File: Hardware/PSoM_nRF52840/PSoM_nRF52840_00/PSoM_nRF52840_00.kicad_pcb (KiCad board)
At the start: 6 copper layers, 26.3 x 23.2 mm, 58 parts, among them J101 DF40C-60DP-0.4V(51), J102 Bare PCB USB C, SW401 SW_Push, SW402 SW_Push, U201 BQ24075RGTR, U301 MIC5528-3.3YMT-T5, U401 ESP32-S2FH4, Y601 Crystal_GND24_Small

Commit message: working on nrf52840
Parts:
- removed C201, C203: 4u7, Capacitor_SMD:C_0603_1608Metric
- removed C202: 1u, Capacitor_SMD:C_0603_1608Metric
- removed C301, C302: 2u2, Capacitor_SMD:C_0603_1608Metric
- removed C401, C402: 15p, Capacitor_SMD:C_0201_0603Metric
- removed C405, C408, C411, C412, C414, C415, C416: 100n, Capacitor_SMD:C_0201_0603Metric
- removed C406, C407: C, Capacitor_SMD:C_0201_0603Metric
- removed C409: 10u, Capacitor_SMD:C_0603_1608Metric
- removed C410, C413: 1u, Capacitor_SMD:C_0402_1005Metric
- removed R1, R2: R, Resistor_SMD:R_0402_1005Metric
- removed R103: 220k, Resistor_SMD:R_0201_0603Metric
- removed R104: 470k, Resistor_SMD:R_0201_0603Metric
- removed R201: 0, Resistor_SMD:R_0402_1005Metric
- removed R202: 36k5, Resistor_SMD:R_0402_1005Metric
- removed R203: 590, Resistor_SMD:R_0402_1005Metric
- removed R204: 1k1, Resistor_SMD:R_0402_1005Metric
- removed R205, R206: 1k5, Resistor_SMD:R_0402_1005Metric
- removed R207: 100k, Resistor_SMD:R_0402_1005Metric
- removed R301: 0k, Resistor_SMD:R_0201_0603Metric
- removed R401: 0, Resistor_SMD:R_0201_0603Metric
- removed R402: 2k, Resistor_SMD:R_0402_1005Metric
- removed R403, R404: 10k, Resistor_SMD:R_0201_0603Metric
- removed R405, R406, R407, R408: nu, Resistor_SMD:R_0201_0603Metric
- removed SW401, SW402: SW_Push, Component_lib:B3U-1000P
- removed U301: MIC5528-3.3YMT-T5, Component_lib:SON40P120X120X60-7N-D
- removed Y601: Crystal_GND24_Small, Component_lib:Crystal_SMD_2016-4Pin_2.0x1.6mm
- added ANT450: 2450AT18A100E, Component_lib:ANTC3216X140N, F.Cu at (163.7, 97.7)
- added C451: 1p, Capacitor_SMD:C_0201_0603Metric, F.Cu at (159.4, 90.2)
- added C461: 100n, Capacitor_SMD:C_0201_0603Metric, F.Cu at (159.4, 91.9)
- added D461: LED, LED_SMD:LED_0402_1005Metric, F.Cu at (172.4, 90.0)
- added L451: 3n9, Inductor_SMD:L_0201_0603Metric, F.Cu at (159.4, 95.4)
- added L452: 2n7, Inductor_SMD:L_0201_0603Metric, F.Cu at (159.4, 97.2)
- added R461: 10k, Resistor_SMD:R_0201_0603Metric, F.Cu at (159.4, 98.9)
- added R462: 2k, Resistor_SMD:R_0402_1005Metric, F.Cu at (172.2, 92.0)
- added SW461: SW_Push, Component_lib:B3U-1000P, F.Cu at (135.7, 106.0)
- added Y401: 830108161301, Component_lib:830108161301_1.6x1.2mm, F.Cu at (172.1, 87.4)
- C101: moved to F.Cu
- C403: value 100n -> 0p8; moved to F.Cu
- C404: value 100n -> 0p5; moved to F.Cu
- L401: value L -> 4n7
- R101: value 5.1k -> 220k; moved to F.Cu
- R102: value 5.1k -> 470k
- U201: value BQ24075RGTR -> NPM1300-QEAA-R; footprint Component_lib:QFN50P300X300X100-17N-D -> Component_lib:NPM1300-QEAA-R
- U401: value ESP32-S2FH4 -> nRF52840-QIAA-aQFN73; footprint Component_lib:QFN40P700X700X90-57N-D -> Component_lib:Nordic_AQFN-73-1EP_7x7mm_P0.5mm; moved to F.Cu
- moved R101 51.6 mm to (176.8, 89.3), turned to 0 degrees
- moved R102 51.0 mm to (176.8, 91.1), turned to 0 degrees
- moved C101 36.3 mm to (176.8, 87.6)
- moved U401 31.8 mm to (165.7, 90.8), turned to 0 degrees
- moved C403 30.8 mm to (159.4, 86.7), turned to 0 degrees
- moved C404 27.0 mm to (159.4, 88.4), turned to 0 degrees
- moved L401 24.0 mm to (159.4, 93.7), turned to 0 degrees
- moved U201 1.58 mm to (142.1, 95.0), turned to -135 degrees
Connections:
- C403 pad 1: +3V3 -> /400-nRF52840/LNA_IN
- C404 pad 1: +3V3 -> /400-nRF52840/ANT_IN
- J101 pad 14: /VSYS -> /100_Connectors/VSYS
- J101 pad 16: /VSYS -> /100_Connectors/VSYS
- J101 pad 28: /100_Connectors/EN -> /100_Connectors/RST
- J101 pad 4: /VBAT -> /100_Connectors/VBAT
- J101 pad 6: /VBAT -> /100_Connectors/VBAT
- J101 pad 8: /VBAT -> /100_Connectors/VBAT
- L401 pad 1: /400_ESP32/ANT -> /400-nRF52840/ANT_IN
- L401 pad 2: /400_ESP32/LNA_IN -> /400-nRF52840/LNA_IN
- R101 pad 1: /100_Connectors/CC2 -> /100_Connectors/VBAT
- R101 pad 2: GND -> IO1
- R102 pad 1: /100_Connectors/CC1 -> IO1
- U201 pad 1: /100_Connectors/BATTERY_TEMP -> /200_1S_Charger/3V3_nRF
- U201 pad 10: /VSYS -> unconnected-(U201-GPIO3-Pad10)
- U201 pad 11: /VSYS -> unconnected-(U201-GPIO4-Pad11)
- U201 pad 12: /200_1S_Charger/ILIM -> /200_1S_Charger/3V3_nRF
- U201 pad 13: VBUS -> /200_1S_Charger/SDA
- U201 pad 14: /200_1S_Charger/TMR -> /200_1S_Charger/SCL
- U201 pad 15: /200_1S_Charger/SYSOFF -> Net-(U201-SHPHLD)
- U201 pad 16: /200_1S_Charger/ISET -> Net-(U201-VSET2)
- U201 pad 17: GND -> Net-(U201-VSET1)
- U201 pad 2: /VBAT -> GND
- U201 pad 3: /VBAT -> /200_1S_Charger/SW1
- U201 pad 4: /200_1S_Charger/BQ_CE -> /100_Connectors/VSYS
- U201 pad 5: /200_1S_Charger/EN2 -> /200_1S_Charger/SW2
- U201 pad 6: /200_1S_Charger/EN1 -> GND
- U201 pad 7: /200_1S_Charger/BQ_PGOOD -> unconnected-(U201-GPIO0-Pad7)
- U201 pad 8: GND -> unconnected-(U201-GPIO1-Pad8)
- U201 pad 9: /200_1S_Charger/BQ_CHG -> unconnected-(U201-GPIO2-Pad9)
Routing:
- net GND: track 96.0 -> 22.2 mm, vias 71 -> 11
- net /VSYS: track 38.2 -> 0.00 mm, vias 4 -> 0
- net +3V3: track 36.4 -> 0.00 mm, vias 13 -> 0
- net VBUS: track 48.9 -> 17.1 mm, vias 5 -> 0
- net /VBAT: track 26.9 -> 0.00 mm, vias 4 -> 0
- net /100_Connectors/EN: track 21.9 -> 0.00 mm, vias 3 -> 0
- net IO15: track 20.4 -> 0.00 mm, vias 2 -> 0
- net IO41: track 17.8 -> 0.00 mm
- net IO40: track 17.6 -> 0.00 mm
- net IO0: track 17.0 -> 0.00 mm, vias 2 -> 0
- net /100_Connectors/RX0: track 16.7 -> 0.00 mm, vias 2 -> 0
- net IO39: track 16.3 -> 0.00 mm
- net /100_Connectors/TX0: track 15.9 -> 0.00 mm, vias 2 -> 0
- net IO37: track 15.3 -> 0.00 mm
- net IO38: track 15.3 -> 0.00 mm
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- removed copper zone on F.Cu, net +3V3
- removed copper zone on In2.Cu, net +3V3
- removed copper zone on F.Cu, net /VBAT
- removed copper zone on F.Cu, net /VSYS
- removed copper zone on B.Cu, net GND
- removed copper zone on F.Cu, net GND

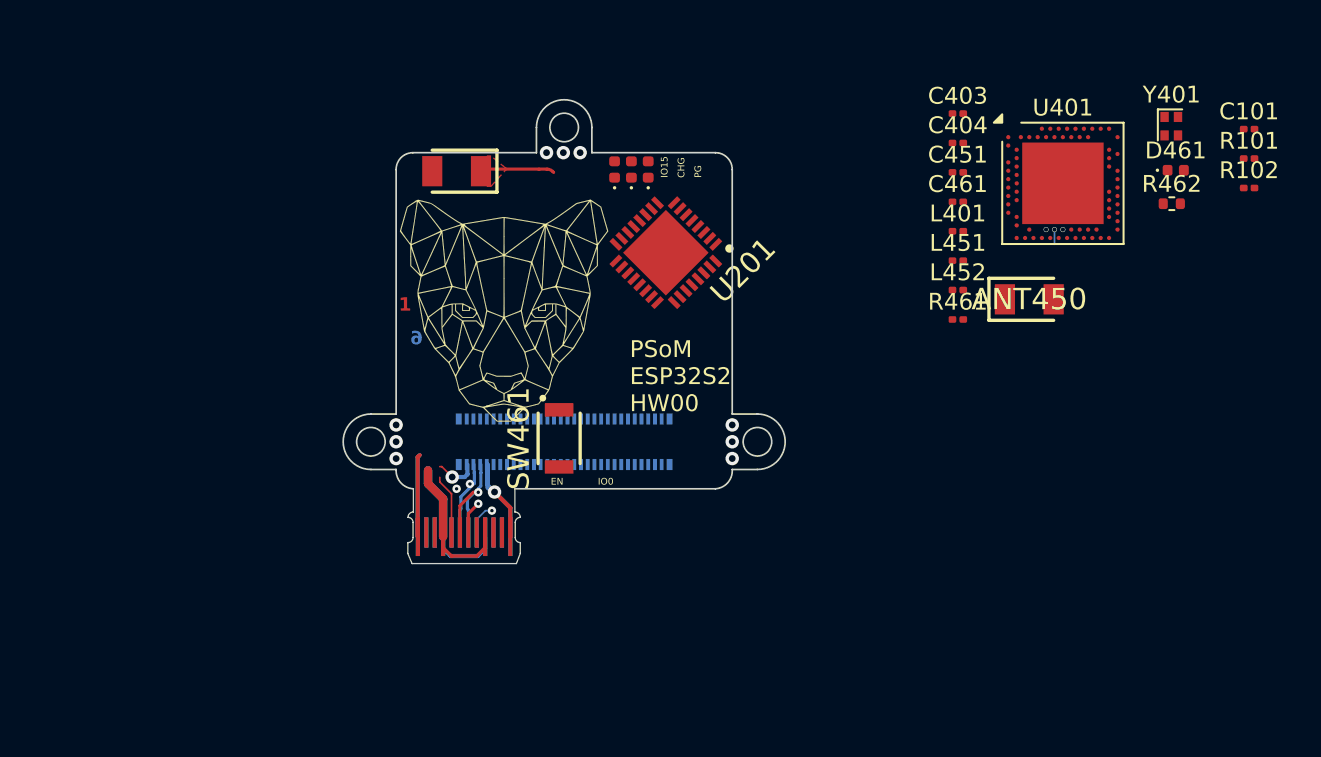
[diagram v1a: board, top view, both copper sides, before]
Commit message: footprint assignement done
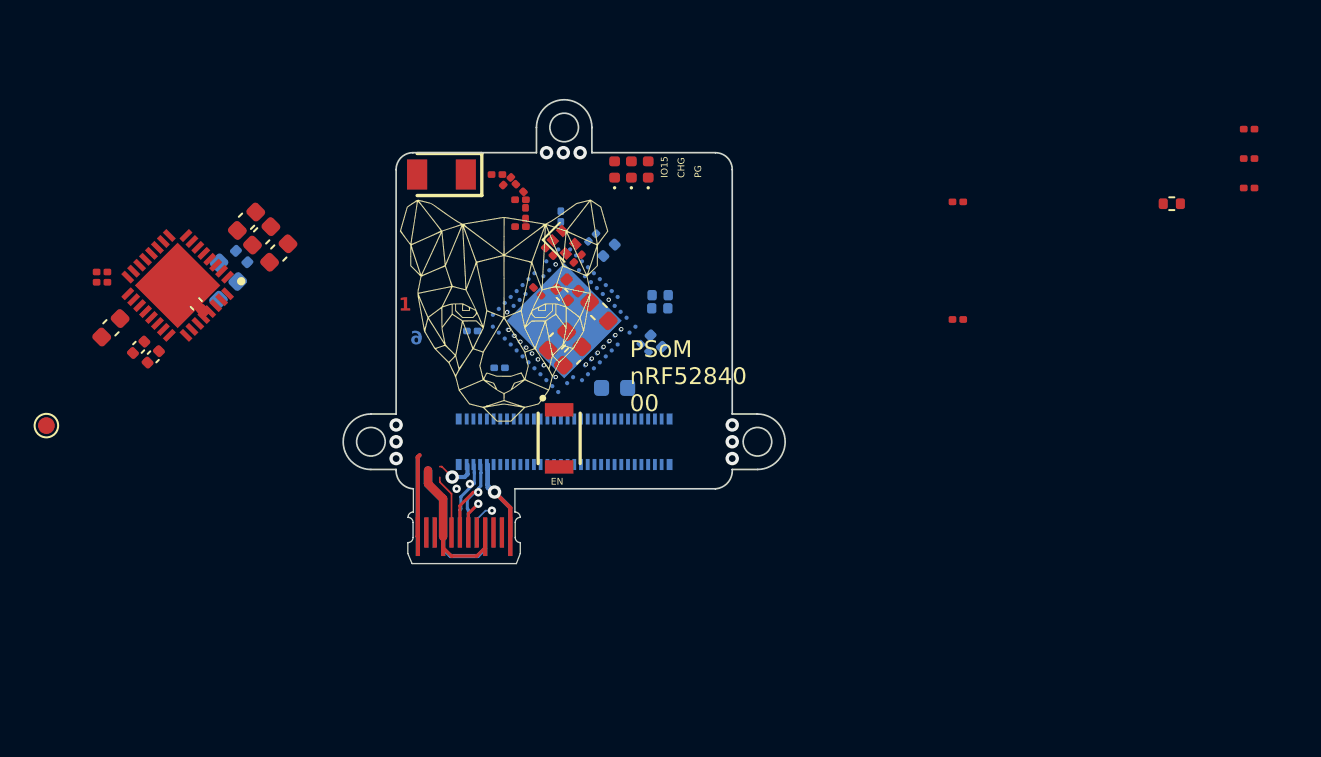
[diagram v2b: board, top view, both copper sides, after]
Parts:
- removed ANT401: 2450AT18A100E, Component_lib:ANTC3216X140N
- removed D401: LED, LED_SMD:LED_0402_1005Metric
- added C201: 1u, Capacitor_SMD:C_0402_1005Metric, F.Cu at (110.7, 100.6)
- added C202: 10u, Capacitor_SMD:C_0603_1608Metric, F.Cu at (117.1, 93.1)
- added C203: 10u, Capacitor_SMD:C_0603_1608Metric, F.Cu at (118.0, 94.0)
- added C204: 10u, Capacitor_SMD:C_0603_1608Metric, F.Cu at (119.0, 95.0)
- added C205: 1u, Capacitor_SMD:C_0402_1005Metric, F.Cu at (111.5, 101.2)
- added C206: 2u2, Capacitor_SMD:C_0603_1608Metric, F.Cu at (109.0, 99.4)
- added C207: 10u, Capacitor_SMD:C_0402_1005Metric, B.Cu at (116.8, 95.2)
- added C208: 10u, Capacitor_SMD:C_0402_1005Metric_Pad0.74x0.62mm_HandSolder, F.Cu at (114.1, 98.0)
- added C401: 12p, Capacitor_SMD:C_0201_0603Metric, F.Cu at (135.1, 94.9)
- added C402: 12p, Capacitor_SMD:C_0201_0603Metric, F.Cu at (136.8, 95.3)
- added C405: 100n, Capacitor_SMD:C_0201_0603Metric, B.Cu at (140.8, 100.6)
- added C406: 4u7, Capacitor_SMD:C_0603_1608Metric, B.Cu at (139.0, 103.0)
- added C407: 100n, Capacitor_SMD:C_0201_0603Metric, B.Cu at (132.2, 101.8)
- added C408: 100n, Capacitor_SMD:C_0201_0603Metric, B.Cu at (130.5, 99.6)
- added C409: 820p, Capacitor_SMD:C_0201_0603Metric, F.Cu at (134.4, 97.2)
- added C410: nc, Capacitor_SMD:C_0402_1005Metric, F.Cu at (135.9, 97.5)
- added C411: 100p, Capacitor_SMD:C_0201_0603Metric, B.Cu at (135.8, 92.8)
- added C412: 100n, Capacitor_SMD:C_0201_0603Metric, B.Cu at (137.7, 94.0)
- added C413: nc, Capacitor_SMD:C_0402_1005Metric, B.Cu at (138.7, 94.8)
- added C414: 1u, Capacitor_SMD:C_0402_1005Metric, B.Cu at (141.5, 100.2)
- added C415: 1u, Capacitor_SMD:C_0402_1005Metric, B.Cu at (141.7, 98.3)
- added C416: 47n, Capacitor_SMD:C_0402_1005Metric, B.Cu at (141.7, 97.5)
- added C420: 4u7, Capacitor_SMD:C_0603_1608Metric, F.Cu at (135.6, 100.2)
- added C421: 4u7, Capacitor_SMD:C_0603_1608Metric, F.Cu at (136.5, 101.1)
- added L201: 2u2, Inductor_SMD:L_0603_1608Metric, B.Cu at (116.0, 96.1)
- added L202: 2u2, Inductor_SMD:L_0603_1608Metric, B.Cu at (114.9, 97.2)
- added L402: 10u, Inductor_SMD:L_0603_1608Metric, F.Cu at (138.1, 98.5)
- added L403: 15n, Inductor_SMD:L_0402_1005Metric, F.Cu at (136.5, 96.9)
- added R203: 47k, Resistor_SMD:R_0201_0603Metric, F.Cu at (108.5, 96.7)
- added R204: 470k, Resistor_SMD:R_0201_0603Metric, F.Cu at (108.5, 96.1)
- added SHIPHLD1: TestPoint, TestPoint:TestPoint_Pad_D1.0mm, F.Cu at (105.2, 105.2)
- U401: moved to B.Cu
- moved Y401 36.8 mm to (136.0, 94.3), turned to 45 degrees
- moved ANT450 35.8 mm to (128.7, 90.3), turned to 180 degrees
- moved D461 33.4 mm to (139.0, 90.0), turned to 90 degrees
- moved U401 30.8 mm to (136.0, 99.0), turned to 135 degrees
- moved U201 29.1 mm to (113.0, 96.9)
- moved L451 27.9 mm to (132.0, 90.3)
- moved L452 27.6 mm to (132.6, 90.7), turned to -135 degrees
- moved C403 26.9 mm to (133.4, 93.4), turned to 180 degrees
- moved C404 26.2 mm to (133.4, 91.8), turned to 180 degrees
- moved C451 26.1 mm to (133.3, 91.1), turned to -45 degrees
- moved L401 25.7 mm to (133.7, 92.6), turned to -90 degrees
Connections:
- U401 pad A10: unconnected-(U401-AIN5/P0.29-PadA10) -> /400-nRF52840/P25
- U401 pad A14: unconnected-(U401-P1.15-PadA14) -> /400-nRF52840/P33
- U401 pad A16: unconnected-(U401-P1.13-PadA16) -> /400-nRF52840/P29
- U401 pad A20: unconnected-(U401-P1.10-PadA20) -> /400-nRF52840/P23
- U401 pad A8: unconnected-(U401-AIN7/P0.31-PadA8) -> /400-nRF52840/P27
- U401 pad G1: unconnected-(U401-P0.26-PadG1) -> /400-nRF52840/P30
- U401 pad H2: unconnected-(U401-P0.27-PadH2) -> /400-nRF52840/P32
- U401 pad R1: unconnected-(U401-TRACEDATA3/P1.09-PadR1) -> /400-nRF52840/P39
- U401 pad U24: unconnected-(U401-P1.04-PadU24) -> /400-nRF52840/P31
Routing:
- net /400_ESP32/ANT: track 4.43 -> 0.00 mm
- net /400-nRF52840/P38: track 0.94 -> 0.04 mm
- net /400-nRF52840/P35: track 0.00 -> 0.08 mm, vias 0 -> 1
- net /400-nRF52840/P11: track 0.00 -> 0.08 mm, vias 0 -> 1
- net /400-nRF52840/P7: track 0.00 -> 0.07 mm, vias 0 -> 1
- net /400-nRF52840/P21: track 0.00 -> 0.07 mm, vias 0 -> 1
- net /400-nRF52840/P44: track 0.00 -> 0.07 mm, vias 0 -> 1
- net /400-nRF52840/P32: track 0.00 -> 0.06 mm, vias 0 -> 1
- net SPI4: track 0.00 -> 0.06 mm, vias 0 -> 1
- net /400-nRF52840/P15: track 0.00 -> 0.06 mm, vias 0 -> 1
- net SPI5: track 0.00 -> 0.06 mm, vias 0 -> 1
- net /400-nRF52840/P46: track 0.00 -> 0.05 mm, vias 0 -> 1
- net /400-nRF52840/P13: track 0.00 -> 0.05 mm, vias 0 -> 1
- net SPI2: track 0.00 -> 0.05 mm, vias 0 -> 1
- net /400-nRF52840/DECUSB: track 0.00 -> 0.03 mm, vias 0 -> 1
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- removed copper zone on F.Cu, net /400_ESP32/ANT
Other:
- board text added: "PSoM nRF52840 00"
- board text removed: "IO0"
- board text removed: "PSoM ESP32S2 HW00"

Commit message: working on schematic
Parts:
- C207, C411, L201, L202: moved to F.Cu
- moved C411 24.4 mm to (143.6, 115.9), turned to -45 degrees
- moved C409 21.3 mm to (141.6, 117.3)
- moved L402 21.0 mm to (144.8, 118.3)
- moved C410 20.8 mm to (142.5, 117.2)
- moved C401 20.8 mm to (142.4, 114.4)
- moved C405 20.8 mm to (148.1, 120.1)
- moved C406 20.8 mm to (146.3, 122.5)
- moved C407 20.8 mm to (139.5, 121.3)
- moved C408 20.8 mm to (137.8, 119.1)
- moved C412 20.8 mm to (145.0, 113.5)
- moved C413 20.8 mm to (146.0, 114.3)
- moved C414 20.8 mm to (148.8, 119.7)
- moved C415 20.8 mm to (149.0, 117.8)
- moved U401 20.8 mm to (143.3, 118.5)
- moved Y401 20.8 mm to (143.3, 113.8)
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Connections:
- net Net-(U201-SHPHLD) renamed /200_1S_Charger/SHIP
- net Net-(U201-VSET1) renamed /200_1S_Charger/VSET1
- net Net-(U201-VSET2) renamed /200_1S_Charger/VSET2
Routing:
- net /200_1S_Charger/3V3_nRF: track 0.00 -> 10.4 mm
- net /100_Connectors/VSYS: track 0.00 -> 6.35 mm
- net /400-nRF52840/DEC4_6: track 0.00 -> 5.07 mm, vias 0 -> 1
- net /200_1S_Charger/VBUS_OUT: track 0.00 -> 3.70 mm, vias 0 -> 1
- net /200_1S_Charger/SW2: track 0.00 -> 3.31 mm
- net /200_1S_Charger/SW1: track 0.00 -> 3.25 mm
- net /100_Connectors/VBAT: track 0.00 -> 2.04 mm
- net /400-nRF52840/DECUSB: track 0.03 -> 2.05 mm
- net /400-nRF52840/DCC: track 0.00 -> 1.90 mm, vias 0 -> 1
- net /200_1S_Charger/VSET1: track 0.00 -> 1.68 mm
- net VBUS: track 17.1 -> 18.6 mm
- net /400-nRF52840/XC2: track 0.00 -> 1.36 mm, vias 0 -> 1
- net /100_Connectors/CC1: track 3.57 -> 4.91 mm
- net /100_Connectors/BATTERY_TEMP: track 0.00 -> 1.33 mm
- net /400-nRF52840/XC1: track 0.00 -> 1.31 mm, vias 0 -> 1
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
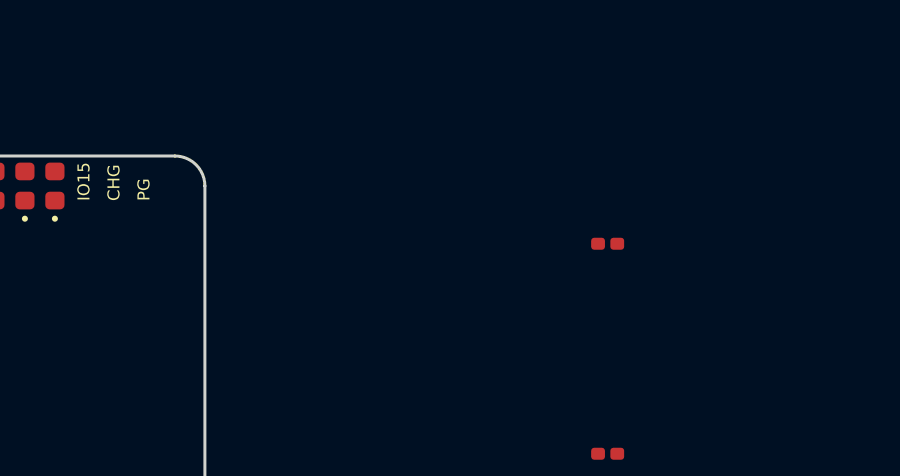
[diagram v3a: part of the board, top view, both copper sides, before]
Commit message: added nfc connector + update pinout info
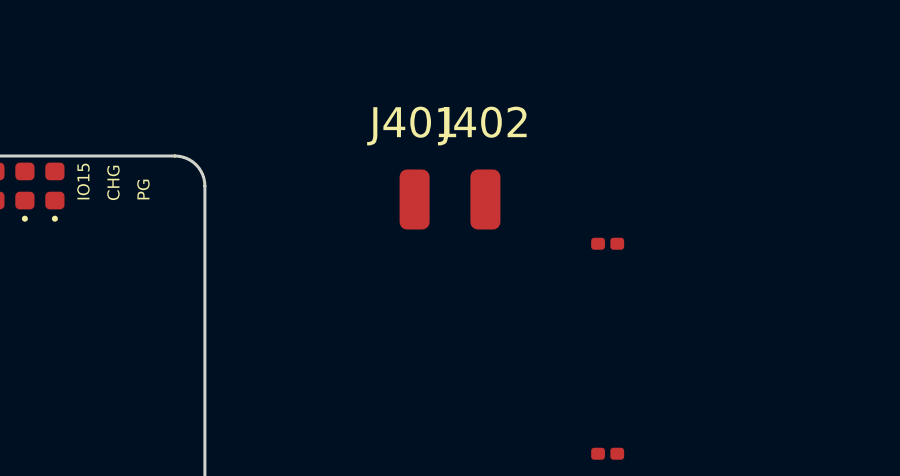
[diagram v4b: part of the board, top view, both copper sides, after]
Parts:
- added J401: Conn_01x01_Pin, Connector_Wire:SolderWirePad_1x01_SMD_1x2mm, F.Cu at (153.0, 90.5)
- added J402: Conn_01x01_Pin, Connector_Wire:SolderWirePad_1x01_SMD_1x2mm, F.Cu at (155.3, 90.5)
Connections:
- net IO0 renamed /100_Connectors/IO0
- C461 pad 1: SPI3 -> /100_Connectors/RST
- J101 pad 11: IO5 -> P11
- J101 pad 13: IO6 -> P13
- J101 pad 15: IO7 -> P15
- J101 pad 17: IO8 -> P17
- J101 pad 19: IO9 -> P19
- J101 pad 21: IO10 -> P21
- J101 pad 23: IO11 -> P23
- J101 pad 25: IO12 -> P25
- J101 pad 27: IO13 -> P27
- J101 pad 29: IO14 -> P29
- J101 pad 30: IO33 -> P30
- J101 pad 31: IO15 -> P31
- J101 pad 32: IO34 -> P32
- J101 pad 33: IO16 -> P33
- J101 pad 34: IO35 -> P34
- J101 pad 35: IO17 -> P35
- J101 pad 36: IO36 -> P36
- J101 pad 37: IO18 -> P37
- J101 pad 38: IO37 -> P38
- J101 pad 39: IO21 -> P39
- J101 pad 40: IO38 -> P40
- J101 pad 42: IO41 -> P42
- J101 pad 44: IO39 -> P44
- J101 pad 46: IO40 -> P46
- J101 pad 48: /100_Connectors/RX0 -> P52
- J101 pad 5: IO2 -> P5
- J101 pad 50: /100_Connectors/TX0 -> unconnected-(J101-Pad50)
- J101 pad 52: IO42 -> unconnected-(J101-Pad52)
- J101 pad 7: IO3 -> P7
- J101 pad 9: IO4 -> P9
- R461 pad 2: SPI3 -> /100_Connectors/RST
- SW461 pad 1: SPI3 -> /100_Connectors/RST
- U401 pad A10: /400-nRF52840/P25 -> P25
- U401 pad A12: /400-nRF52840/VBAT_VOLTAGE_DIVIDER -> unconnected-(U401-AIN0/P0.02-PadA12)
- U401 pad A14: /400-nRF52840/P33 -> P33
- U401 pad A16: /400-nRF52840/P29 -> P29
- U401 pad A20: /400-nRF52840/P23 -> P23
- U401 pad A8: /400-nRF52840/P27 -> P27
- U401 pad AC11: /400-nRF52840/P38 -> P38
- U401 pad AC13: SPI3 -> /100_Connectors/RST
- U401 pad AC21: /400-nRF52840/P44 -> P44
- U401 pad AC9: /400-nRF52840/P34 -> P34
- U401 pad AD10: /400-nRF52840/P36 -> P36
- U401 pad AD12: /400-nRF52840/P40 -> P40
- U401 pad AD20: /400-nRF52840/P42 -> P42
- U401 pad B9: /400-nRF52840/P17 -> P17
- U401 pad D2: /400-nRF52840/P13 -> P13
- U401 pad F2: /400-nRF52840/P15 -> P15
- U401 pad G1: /400-nRF52840/P30 -> P30
- U401 pad H2: /400-nRF52840/P32 -> P32
- U401 pad J1: /400-nRF52840/P19 -> P19
- U401 pad J24: unconnected-(U401-NFC2/P0.10-PadJ24) -> /400-nRF52840/NFC2
- U401 pad K2: /400-nRF52840/P21 -> P21
- U401 pad L1: /400-nRF52840/P5 -> P5
- U401 pad L24: unconnected-(U401-NFC1/P0.09-PadL24) -> /400-nRF52840/NFC1
- U401 pad M2: /400-nRF52840/P7 -> P7
- U401 pad N1: /400-nRF52840/P9 -> P9
- U401 pad P2: /400-nRF52840/P11 -> P11
- U401 pad R1: /400-nRF52840/P39 -> P39
- U401 pad T2: /400-nRF52840/P35 -> P35
- U401 pad U1: /400-nRF52840/P37 -> P37
- U401 pad U24: /400-nRF52840/P31 -> P31
- U401 pad W24: /400-nRF52840/P52 -> P52
- U401 pad Y23: /400-nRF52840/P46 -> P46
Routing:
- net SPI3: track 1.10 -> 0.00 mm, vias 1 -> 0
- net /100_Connectors/RST: track 0.00 -> 1.10 mm, vias 0 -> 1
- net P35: track 0.00 -> 0.08 mm, vias 0 -> 1
- net /400-nRF52840/P35: track 0.08 -> 0.00 mm, vias 1 -> 0
- net P11: track 0.00 -> 0.08 mm, vias 0 -> 1
- net /400-nRF52840/P11: track 0.08 -> 0.00 mm, vias 1 -> 0
- net P7: track 0.00 -> 0.07 mm, vias 0 -> 1
- net /400-nRF52840/P7: track 0.07 -> 0.00 mm, vias 1 -> 0
- net P21: track 0.00 -> 0.07 mm, vias 0 -> 1
- net /400-nRF52840/P21: track 0.07 -> 0.00 mm, vias 1 -> 0
- net P44: track 0.00 -> 0.07 mm, vias 0 -> 1
- net /400-nRF52840/P44: track 0.07 -> 0.00 mm, vias 1 -> 0
- net P32: track 0.00 -> 0.06 mm, vias 0 -> 1
- net /400-nRF52840/P32: track 0.06 -> 0.00 mm, vias 1 -> 0
- net P15: track 0.00 -> 0.06 mm, vias 0 -> 1
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
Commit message: moved in the nrf inside of boundries
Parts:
- moved L201 36.0 mm to (143.7, 93.0), turned to 180 degrees
- moved C207 35.1 mm to (144.8, 94.9), turned to -90 degrees
- moved C208 35.0 mm to (140.9, 91.9), turned to 180 degrees
- moved C202 34.2 mm to (143.0, 94.1), turned to 0 degrees
- moved L202 33.7 mm to (140.9, 93.0), turned to 180 degrees
- moved C203 31.9 mm to (140.3, 94.1), turned to 180 degrees
- moved U201 28.5 mm to (141.4, 98.0), turned to -90 degrees
- moved C205 26.0 mm to (142.7, 102.4), turned to -90 degrees
- moved C201 25.0 mm to (141.9, 102.4), turned to 90 degrees
- moved C204 23.4 mm to (140.8, 102.8), turned to -90 degrees
- moved R204 22.8 mm to (137.8, 100.2), turned to 180 degrees
- moved C401 22.6 mm to (131.4, 94.7)
- moved C410 22.6 mm to (131.5, 97.5)
- moved C411 22.6 mm to (132.6, 96.2)
- moved C421 22.6 mm to (133.0, 100.7)
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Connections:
- J101 pad 48: P52 -> /100_Connectors/SWDCLK
- J101 pad 50: unconnected-(J101-Pad50) -> /100_Connectors/SWDIO
- J101 pad 52: unconnected-(J101-Pad52) -> P52
